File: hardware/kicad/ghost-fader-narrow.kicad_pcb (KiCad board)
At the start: 2 copper layers, 156 x 74.5 mm, 74 parts, among them J1 NRJ6HF, J2 NRJ6HF, J3 NRJ6HF, J4 NRJ6HF, SW1 MIDI channel, U1 THAT1246S08, U2 THAT1246S08, U3 PGA2310PA, U4 PGA2310PA, U5 OPA2134PA, U6 THAT1646S08, U7 THAT1646S08, U9 Teensy 4.0

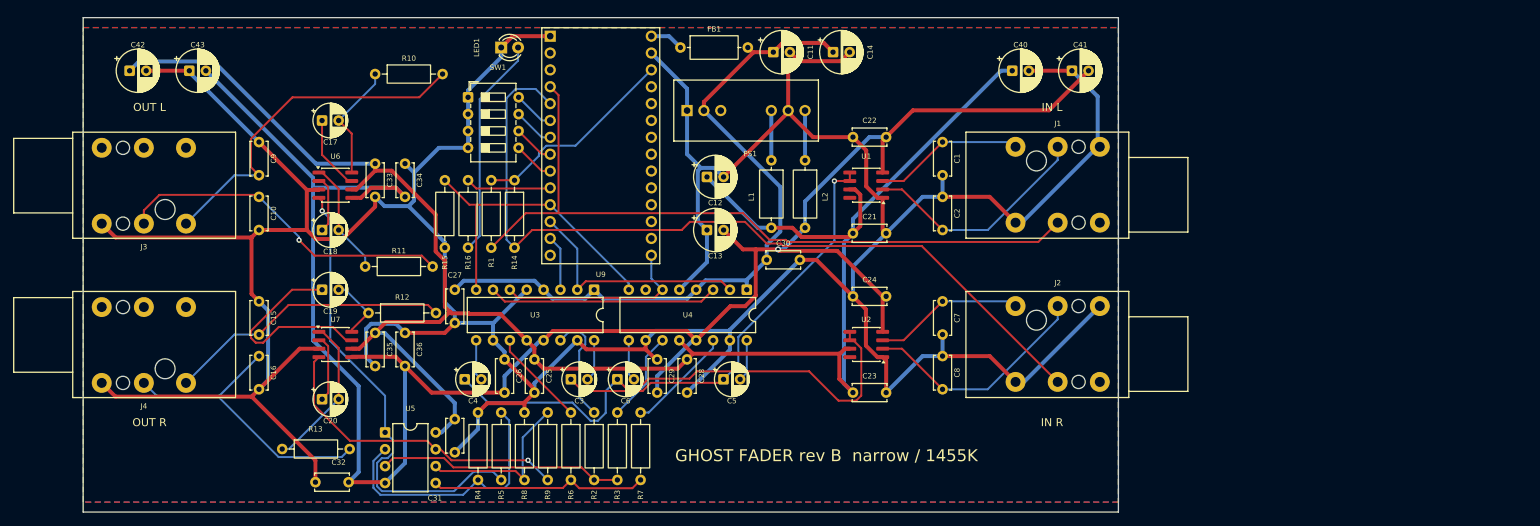
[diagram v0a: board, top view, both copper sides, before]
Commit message: Make the 207 x 38 mm board the narrow PCB, replacing the 1455K one
The slim board from #4 merged into #3's branch instead of main, so it
never reached the site. This puts it on main under the narrow name and
drops the 156 x 74.5 mm Hammond 1455K1601 board: one narrow board, the
one as wide as two side-by-side jacks allow.

- ghost-fader-narrow.kicad_pcb / .kicad_pro and tools/build_pcb_narrow.py
  are now the 207 x 38 mm board (silkscreen title says narrow).
- Gerbers, zip, renders and copper SVGs regenerated under the narrow name.
- README and site: the narrow section describes this board and the
  3D-printed box it needs; the 1455K text is gone.

The 1590BB board is unchanged. DRC: 0 unconnected, 0 errors.

Co-Authored-By: Claude Fable 5.1 <noreply@anthropic.com>
Claude-Session: https://claude.ai/code/session_01DHZbsBNY11SbG5z1o7yrWX
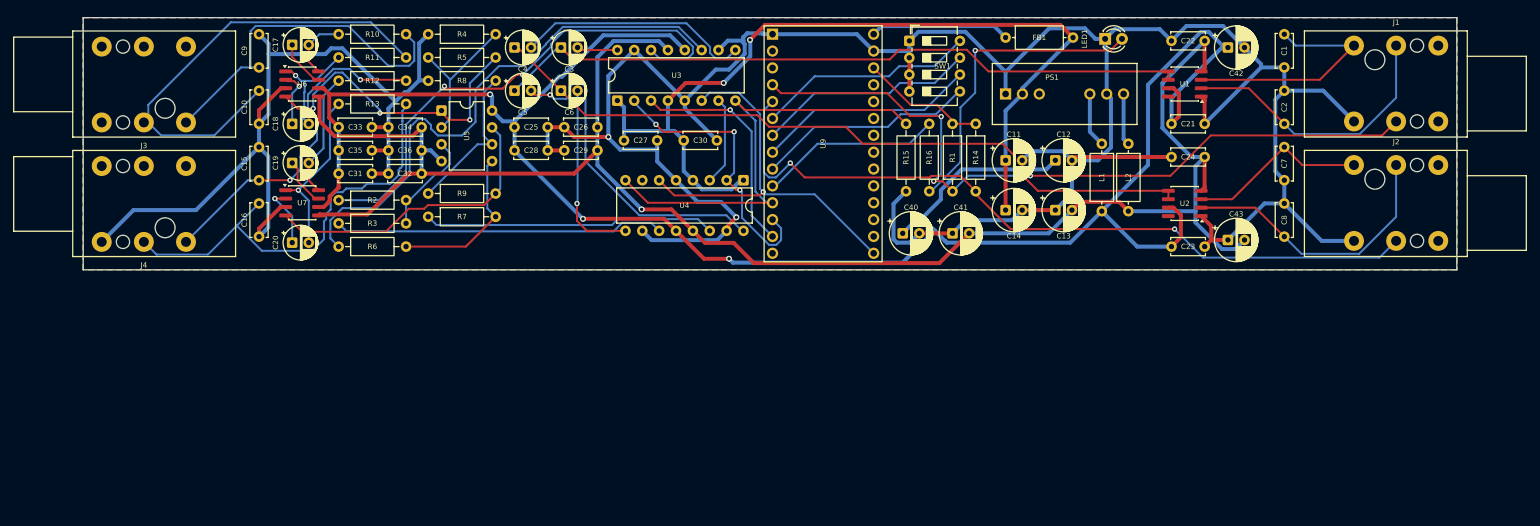
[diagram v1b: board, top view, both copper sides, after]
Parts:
- moved C42 165.5 mm to (172.5, 4.50)
- moved C43 158.6 mm to (172.5, 33.5)
- moved LED1 91.0 mm to (154.0, 3.20)
- moved R1 70.0 mm to (131.0, 16.0)
- moved R14 70.0 mm to (134.5, 16.0)
- moved R15 70.0 mm to (124.0, 16.0)
- moved R16 70.0 mm to (127.5, 16.0)
- moved SW1 67.0 mm to (124.5, 3.50)
- moved R4 57.5 mm to (52.0, 2.50), turned to 0 degrees
- moved C7 56.5 mm to (181.0, 19.5)
- moved C8 56.4 mm to (181.0, 28.0)
- moved J2 55.2 mm to (191.5, 22.2)
- moved R5 54.6 mm to (52.0, 6.00), turned to 0 degrees
- moved C1 54.0 mm to (181.0, 2.50)
- moved C2 53.9 mm to (181.0, 11.0)
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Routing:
- net GND: track 616.1 -> 521.3 mm, vias 0 -> 2
- net Net-(U3-VOUTR): track 14.7 -> 83.4 mm
- net Net-(U3-VOUTL): track 17.2 -> 77.9 mm, vias 0 -> 2
- net -15V: track 309.4 -> 260.6 mm
- net Net-(U4-VINL): track 6.29 -> 50.1 mm, vias 0 -> 1
- net L_SE: track 64.9 -> 105.2 mm, vias 1 -> 0
- net Net-(U4-VOUTR): track 13.7 -> 49.8 mm
- net SCLK: track 29.9 -> 59.9 mm, vias 0 -> 1
- net Net-(U3-VINR): track 6.20 -> 35.5 mm
- net R_SE: track 81.1 -> 109.8 mm
- net Net-(U4-VOUTL): track 16.1 -> 44.0 mm
- net Net-(U9-4): track 6.21 -> 33.1 mm
- net Net-(U9-5): track 6.21 -> 33.1 mm
- net Net-(U9-7): track 6.21 -> 33.1 mm
- net Net-(U9-6): track 6.21 -> 33.1 mm
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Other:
- board size 156 x 74.5 mm -> 207 x 38 mm
- board text added: "GHOST FADER rev B narrow"
- board text removed: "GHOST FADER rev B narrow / 1455K"

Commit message: Rev C: XIAO RP2040 and Traco TBA 2-0522 replace the Teensy 4.0 and TMR 3
Tier 1 cost-down, no change to the audio path. U9 becomes a Seeed XIAO
RP2040 on header pins (USB-C, TinyUSB MIDI, its 5V pin is VBUS straight
through), PS1 becomes a 2 W unregulated Traco TBA 2-0522 on KiCad's stock
SIP-7 footprint. Rails are now +/-12 V: the +/-15 V TBA 2-0523 would pass
the PGA2310's 16 V absolute maximum at light load. Parts cost drops from
about $145 to about $110.

- gen.py: TBA2_Dual and XIAO_RP2040 symbols, XIAO footprint (Seeed pin
  numbering, USB-C overhang drawn), control sheet rewired to D0-D10,
  power sheet and notes for the unregulated converter, +/-12V rails.
- check.py: new U9 / PS1 pins; NETLIST OK. ERC 0/0.
- Both boards rebuilt and re-routed (Freerouting 1.9), DRC 0 errors; the
  only warnings are jack-nose and USB-C shell silk over the board edge.
- Gerbers, drill, zips, BOM, schematic SVG/PDF and board renders
  regenerated. README and site updated: pin map, power budget
  (~250 mA typical), level budget at +/-12 V, parts list and totals.

Co-Authored-By: Claude Fable 5.1 <noreply@anthropic.com>
Claude-Session: https://claude.ai/code/session_01C8uqpe49go1TPWMsWKKVkn
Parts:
- PS1: value TMR 3-0523 -> TBA 2-0522; footprint GhostFader:TRACO_TMR3_SIP8 -> Converter_DCDC:Converter_DCDC_TRACO_TBA2-xxxx_Dual_THT
- U9: value Teensy 4.0 -> XIAO RP2040; footprint GhostFader:Teensy40_Edge -> GhostFader:XIAO_RP2040_THT
- moved U9 7.70 mm to (111.5, 11.3)
- moved PS1 1.50 mm to (139.0, 10.0), turned to 90 degrees
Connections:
- net +15V renamed +12V
- net -15V renamed -12V
- PS1 pad 1: GND -> +5V
- PS1 pad 2: +5V -> GND
- SW1 pad 5: Net-(U9-7) -> Net-(U9-D5/SCL/GP7)
- SW1 pad 6: Net-(U9-6) -> Net-(U9-D4/SDA/GP6)
- SW1 pad 7: Net-(U9-5) -> Net-(U9-D3/GP29)
- SW1 pad 8: Net-(U9-4) -> Net-(U9-D2/GP28)
- U9 pad 1: GND -> SENSE_L
- U9 pad 11: ~{MUTE} -> SDI
- U9 pad 12: ~{CS} -> +3V3
- U9 pad 13: SDI -> GND
- U9 pad 14: unconnected-(U9-12-Pad14) -> USB_5V
- U9 pad 2: unconnected-(U9-0-Pad2) -> SENSE_R
- U9 pad 3: unconnected-(U9-1-Pad3) -> Net-(U9-D2/GP28)
- U9 pad 4: SENSE_L -> Net-(U9-D3/GP29)
- U9 pad 5: SENSE_R -> Net-(U9-D4/SDA/GP6)
- U9 pad 6: Net-(U9-4) -> Net-(U9-D5/SCL/GP7)
- U9 pad 7: Net-(U9-5) -> ~{MUTE}
- U9 pad 8: Net-(U9-6) -> ~{CS}
- U9 pad 9: Net-(U9-7) -> SCLK
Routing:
- net GND: track 521.3 -> 557.3 mm, vias 2 -> 1
- net Net-(U9-D2/GP28): track 0.00 -> 35.1 mm, vias 0 -> 1
- net +12V: track 300.2 -> 266.4 mm
- net Net-(U9-5): track 33.1 -> 0.00 mm
- net Net-(U9-4): track 33.1 -> 0.00 mm
- net Net-(U9-7): track 33.1 -> 0.00 mm
- net Net-(U9-6): track 33.1 -> 0.00 mm
- net Net-(U9-D5/SCL/GP7): track 0.00 -> 30.4 mm
- net Net-(U9-D4/SDA/GP6): track 0.00 -> 30.4 mm
- net Net-(U9-D3/GP29): track 0.00 -> 30.4 mm
- net ~{CS}: track 43.4 -> 63.2 mm, vias 3 -> 0
- net LED: track 27.5 -> 9.27 mm
- net +5V: track 134.2 -> 119.0 mm, vias 2 -> 1
- net ~{MUTE}: track 69.0 -> 54.5 mm
- net Net-(C16-Pad1): track 66.3 -> 55.3 mm
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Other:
- board text added: "GHOST FADER rev C narrow"
- board text removed: "GHOST FADER rev B narrow"

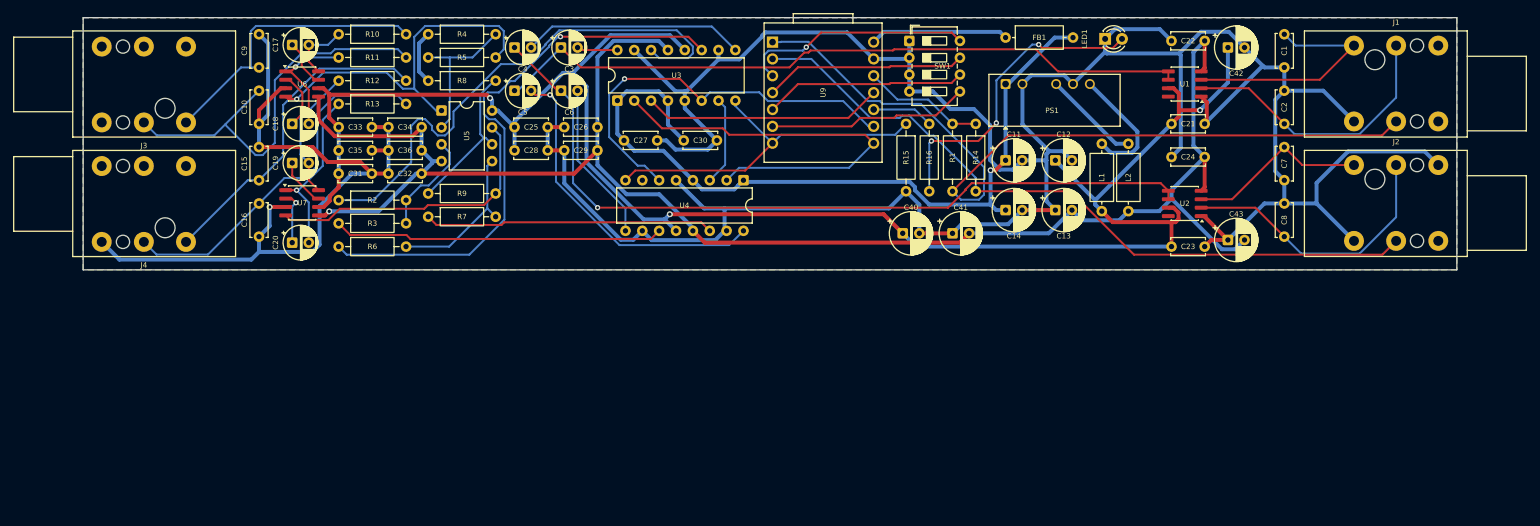
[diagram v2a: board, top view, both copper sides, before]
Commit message: Rev D: isolate the audio ground from USB
Add a TI ISO7762FDW digital isolator on the four control lines and two
plug-sense lines, a 78L05 that makes +5VA from +12 V for the PGA logic
and the isolator's audio side, and a split ground: GND_USB (XIAO, USB-C,
switch, LED, ferrite, reservoir, DC-DC input) and GND (everything audio).
The two meet only through C45 (1 nF) and R17 (1 M) at PS1. The sense
pull-ups drop from 1 M to 100 k for the isolator's input leakage.

Both boards get two ground pours per layer with a 2 mm copper-free gap
and a rule area that keeps the router out; U8 and PS1 straddle the gap.
The 1590BB board's island is the front-left corner; the narrow board's
is a pocket under the XIAO with the audio ground wrapping beneath it.
ERC 0, netlist checked (61 nets, 263 pins), DRC clean on both routed
boards, and a script check confirms no copper crosses the gap.

README, docs page, schematic exports, renders, gerbers and BOM regenerated.

Co-Authored-By: Claude Fable 5.1 <noreply@anthropic.com>
Claude-Session: https://claude.ai/code/session_013C8baRPktSQjwfdzSRwmAq
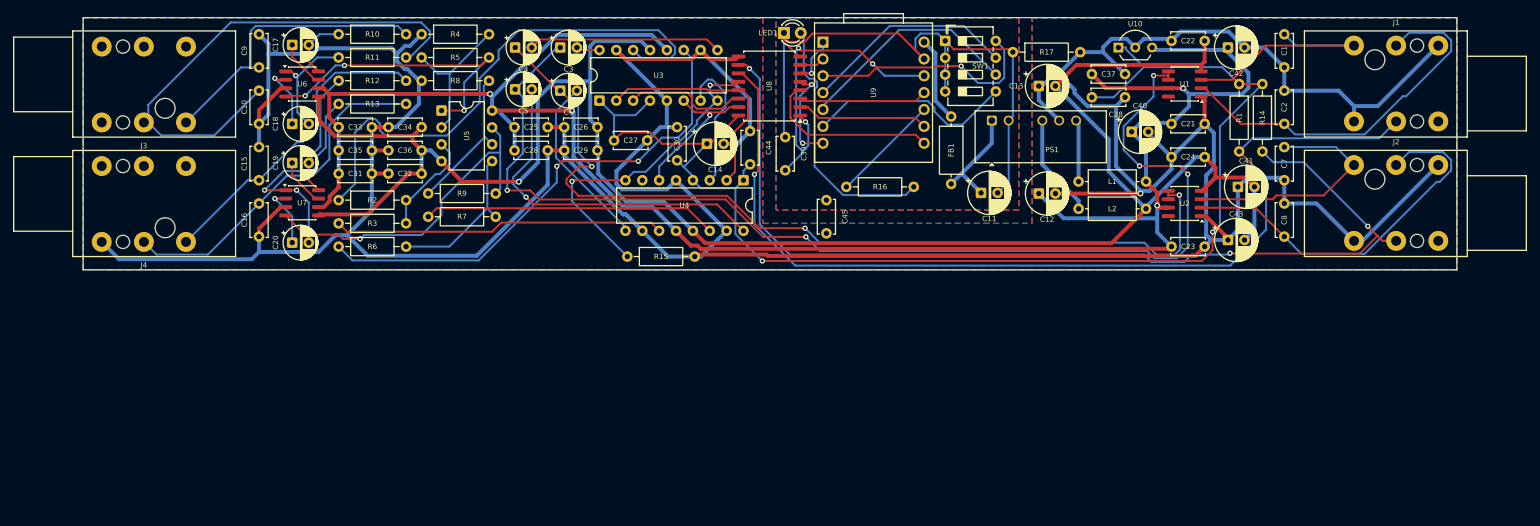
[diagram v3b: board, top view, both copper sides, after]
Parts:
- added C37: 100n, Capacitor_THT:C_Disc_D5.0mm_W2.5mm_P5.00mm, F.Cu at (152.0, 8.50)
- added C38: 100n, Capacitor_THT:C_Disc_D5.0mm_W2.5mm_P5.00mm, F.Cu at (152.0, 12.0)
- added C39: 100n, Capacitor_THT:C_Disc_D5.0mm_W2.5mm_P5.00mm, F.Cu at (105.8, 23.0)
- added C44: 100n, Capacitor_THT:C_Disc_D5.0mm_W2.5mm_P5.00mm, F.Cu at (100.5, 22.1)
- added C45: 1n 1kV, Capacitor_THT:C_Disc_D5.0mm_W2.5mm_P5.00mm, F.Cu at (112.0, 27.5)
- added R17: 1M, Resistor_THT:R_Axial_DIN0207_L6.3mm_D2.5mm_P10.16mm_Horizontal, F.Cu at (140.1, 5.20)
- added U10: L78L05, Package_TO_SOT_THT:TO-92_Inline_Wide, F.Cu at (156.0, 4.50)
- added U8: ISO7762FDW, Package_SO:SOIC-16W_7.5x10.3mm_P1.27mm, F.Cu at (103.4, 10.3)
- R1, R14: value 1M -> 100k
- moved LED1 48.4 mm to (105.6, 2.30)
- moved R15 46.5 mm to (82.0, 36.0), turned to 0 degrees
- moved C14 46.1 mm to (94.0, 19.0)
- moved R1 43.6 mm to (174.2, 10.0)
- moved R14 43.6 mm to (177.7, 10.0)
- moved C41 43.6 mm to (174.0, 25.5)
- moved C40 37.7 mm to (158.0, 17.2)
- moved C13 18.9 mm to (144.0, 10.3)
- moved R16 15.7 mm to (115.0, 25.5), turned to 0 degrees
- moved FB1 14.5 mm to (130.8, 14.9), turned to -90 degrees
- moved L2 12.3 mm to (150.0, 28.8), turned to 0 degrees
- moved U9 7.60 mm to (119.1, 11.3)
- moved L1 6.69 mm to (150.0, 24.7), turned to 0 degrees
- moved C11 6.14 mm to (135.3, 26.4)
- moved PS1 5.88 mm to (136.9, 15.5)
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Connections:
- C11 pad 2: GND -> GND_USB
- C14 pad 1: +5V -> +5VA
- C27 pad 1: +5V -> +5VA
- C30 pad 1: +5V -> +5VA
- LED1 pad 1: GND -> GND_USB
- PS1 pad 2: GND -> GND_USB
- R1 pad 1: +3V3 -> +5VA
- R14 pad 1: +3V3 -> +5VA
- SW1 pad 1: GND -> GND_USB
- SW1 pad 2: GND -> GND_USB
- SW1 pad 3: GND -> GND_USB
- SW1 pad 4: GND -> GND_USB
- U3 pad 1: +5V -> +5VA
- U3 pad 4: +5V -> +5VA
- U4 pad 1: +5V -> +5VA
- U4 pad 4: +5V -> +5VA
- U9 pad 1: SENSE_L -> /Control/MCU_SENSE_L
- U9 pad 11: SDI -> /Control/MCU_SDI
- U9 pad 13: GND -> GND_USB
- U9 pad 2: SENSE_R -> /Control/MCU_SENSE_R
- U9 pad 7: ~{MUTE} -> /Control/MCU_~{MUTE}
- U9 pad 8: ~{CS} -> /Control/MCU_~{CS}
- U9 pad 9: SCLK -> /Control/MCU_SCLK
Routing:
- net +5VA: track 0.00 -> 198.5 mm, vias 0 -> 2
- net +5V: track 119.0 -> 16.2 mm, vias 1 -> 0
- net GND_USB: track 0.00 -> 93.5 mm
- net GND: track 557.3 -> 626.6 mm
- net L_SE: track 106.2 -> 172.3 mm, vias 0 -> 5
- net SENSE_R: track 108.5 -> 148.8 mm, vias 0 -> 3
- net SCLK: track 61.5 -> 22.9 mm
- net -12V: track 252.7 -> 289.3 mm
- net +12V: track 266.4 -> 299.6 mm, vias 3 -> 4
- net +3V3: track 18.4 -> 47.0 mm, vias 0 -> 3
- net ~{CS}: track 63.2 -> 35.1 mm
- net /Control/MCU_~{CS}: track 0.00 -> 26.8 mm
- net SENSE_L: track 120.7 -> 145.5 mm, vias 0 -> 2
- net /Control/MCU_SCLK: track 0.00 -> 19.9 mm
- net /Control/MCU_SDI: track 0.00 -> 19.3 mm
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- added copper zone on B.Cu, net GND_USB
- added copper zone on F.Cu, net GND_USB
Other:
- board text added: "AUDIO GND"
- board text added: "GHOST FADER rev D narrow"
- board text added: "USB GND"
- board text removed: "GHOST FADER rev C narrow"
